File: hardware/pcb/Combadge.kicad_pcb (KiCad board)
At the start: 2 copper layers, 33.7 x 31 mm, 38 parts, among them J1 Conn_01x02_Socket, J2 Conn_01x01_Socket, J3 TOUCH, J4 USB_B_Micro, SW1 SW_Push, SW2 CSS-1210TB, U1 ESP32-WROOM-32, U2 MAX98357AETE+T, U3 MCP73831-2-OT, U4 TL431DBZ, U5 TLV73333PDBV

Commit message: Miscellaneous cleanup
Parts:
- renumbered BT to BT1
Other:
- board text added: "It is possible to commit no mistakes and still lose."
- board text added: "That is not a weakness; that is life."
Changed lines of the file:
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@@
     (property "ki_keywords" "battery cell")
     (attr through_hole)
-    (fp_text reference "BT" (at -2.433971 1.097635 63) (layer "F.SilkS")
+    (fp_text reference "BT1" (at -2.816662 0.066821 63) (layer "F.SilkS")
         (effects (font (size 1 1) (thickness 0.15)))
     )
@@
     (property "ki_keywords" "diode device shunt regulator")
     (attr smd)
-    (fp_text reference "U4" (at -0.0231 2.606) (layer "B.SilkS")
+    (fp_text reference "U4" (at -3.0203 1.0312) (layer "B.SilkS")
         (effects (font (size 1 1) (thickness 0.15)) (justify mirror))
     )
@@
     (property "ki_keywords" "R res resistor")
     (attr smd)
-    (fp_text reference "R2" (at -4.064 0 90) (layer "B.SilkS")
+    (fp_text reference "R2" (at -3.429 -0.4826 90) (layer "B.SilkS")
         (effects (font (size 1 1) (thickness 0.15)) (justify mirror))
     )
@@
     (effects (font (size 1 0.6) (thickness 0.15)) (justify mirror))
   )
+  (gr_text "That is not a weakness;\nthat is life." (at 157.9372 101.092) (layer "B.SilkS")
+    (effects (font (size 0.7 0.7) (thickness 0.16) bold) (justify left bottom mirror))
+  )
   (gr_text "+" (at 165.481 83.058 62) (layer "B.SilkS")
     (effects (font (size 0.8 0.8) (thickness 0.15)) (justify mirror))
@@
     (effects (font (size 0.8 0.8) (thickness 0.125)) (justify mirror))
   )
+  (gr_text "It is possible to\ncommit no mistakes\nand still lose." (at 156.0576 98.552) (layer "B.SilkS")
+    (effects (font (size 0.7 0.7) (thickness 0.16) bold) (justify left bottom mirror))
+  )
   (gr_text "\n+" (at 169.799 102.8446 -225) (layer "F.SilkS")
     (effects (font (size 1 1) (thickness 0.1)))
@@
   (segment (start 147.164 104.0294) (end 147.164 105.2409) (width 0.25) (layer "F.Cu") (net 3))
   (segment (start 160.2105 101.1555) (end 160.147 101.219) (width 0.25) (layer "F.Cu") (net 3))
+  (segment (start 153.2636 107.7468) (end 150.876 107.7468) (width 0.25) (layer "F.Cu") (net 3))
   (segment (start 160.147 101.219) (end 148.082 101.219) (width 0.25) (layer "F.Cu") (net 3))
   (segment (start 153.5445 106.5414) (end 157.443 106.5414) (width 0.25) (layer "F.Cu") (net 3))
+  (segment (start 150.876 109.3984) (end 150.876 107.7468) (width 0.25) (layer "F.Cu") (net 3))
   (segment (start 157.443 106.5414) (end 158.75 107.8484) (width 0.25) (layer "F.Cu") (net 3))
-  (segment (start 152.553 107.7214) (end 153.289 107.7214) (width 0.25) (layer "F.Cu") (net 3))
-  (segment (start 148.6285 107.1509) (end 150.876 109.3984) (width 0.25) (layer "F.Cu") (net 3))
   (segment (start 147.164 105.2409) (end 148.6285 106.7054) (width 0.25) (layer "F.Cu") (net 3))
   (segment (start 170.4594 93.345) (end 170.7896 93.6752) (width 0.25) (layer "F.Cu") (net 3))
   (segment (start 153.289 106.4129) (end 153.289 107.7214) (width 0.25) (layer "F.Cu") (net 3))
   (segment (start 170.7896 93.6752) (end 170.7896 94.5896) (width 0.25) (layer "F.Cu") (net 3))
+  (segment (start 153.289 107.7214) (end 153.2636 107.7468) (width 0.25) (layer "F.Cu") (net 3))
   (segment (start 153.289 106.2859) (end 153.5445 106.5414) (width 0.25) (layer "F.Cu") (net 3))
   (segment (start 169.0755 93.345) (end 170.4594 93.345) (width 0.25) (layer "F.Cu") (net 3))
   (segment (start 147.164 102.137) (end 147.164 104.0294) (width 0.25) (layer "F.Cu") (net 3))
-  (segment (start 148.6285 106.7054) (end 148.6285 107.1509) (width 0.25) (layer "F.Cu") (net 3))
-  (segment (start 150.876 109.3984) (end 152.553 107.7214) (width 0.25) (layer "F.Cu") (net 3))
+  (segment (start 149.6699 107.7468) (end 148.6285 106.7054) (width 0.25) (layer "F.Cu") (net 3))
   (segment (start 169.0755 93.345) (end 169.0755 95.758) (width 0.25) (layer "F.Cu") (net 3))
+  (segment (start 150.876 107.7468) (end 149.6699 107.7468) (width 0.25) (layer "F.Cu") (net 3))
   (segment (start 148.082 101.219) (end 147.164 102.137) (width 0.25) (layer "F.Cu") (net 3))
   (via (at 153.289 107.7214) (size 0.8) (drill 0.4) (layers "F.Cu" "B.Cu") (net 3))

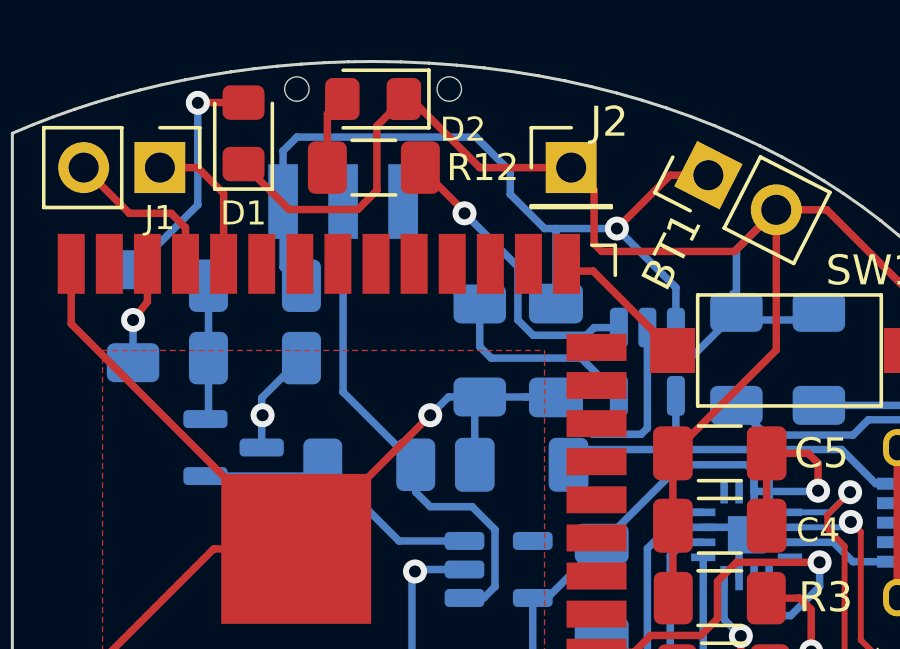
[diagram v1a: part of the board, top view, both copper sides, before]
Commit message: Rewire power switch so that the unit can be turned on
Thank you to Reddit user justadiode.
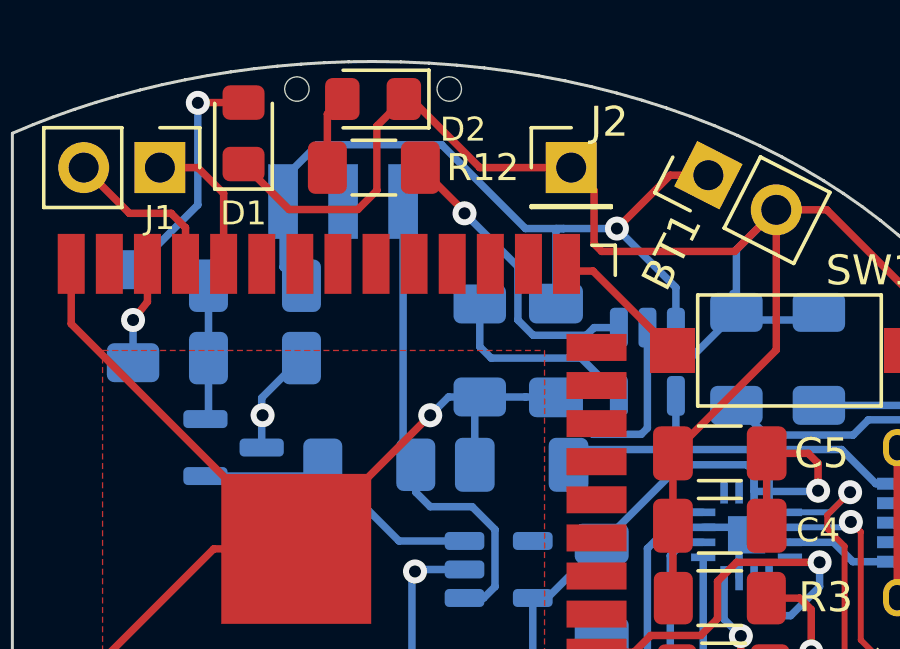
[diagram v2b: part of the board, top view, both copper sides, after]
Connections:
- SW2 pad 2: Net-(U5-IN) -> unconnected-(SW2-Pad2)
- SW2 pad 3: unconnected-(SW2-Pad3) -> Net-(U5-IN)
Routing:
- net +BATT: track 28.2 -> 27.2 mm
- net Net-(U5-IN): track 16.9 -> 16.1 mm

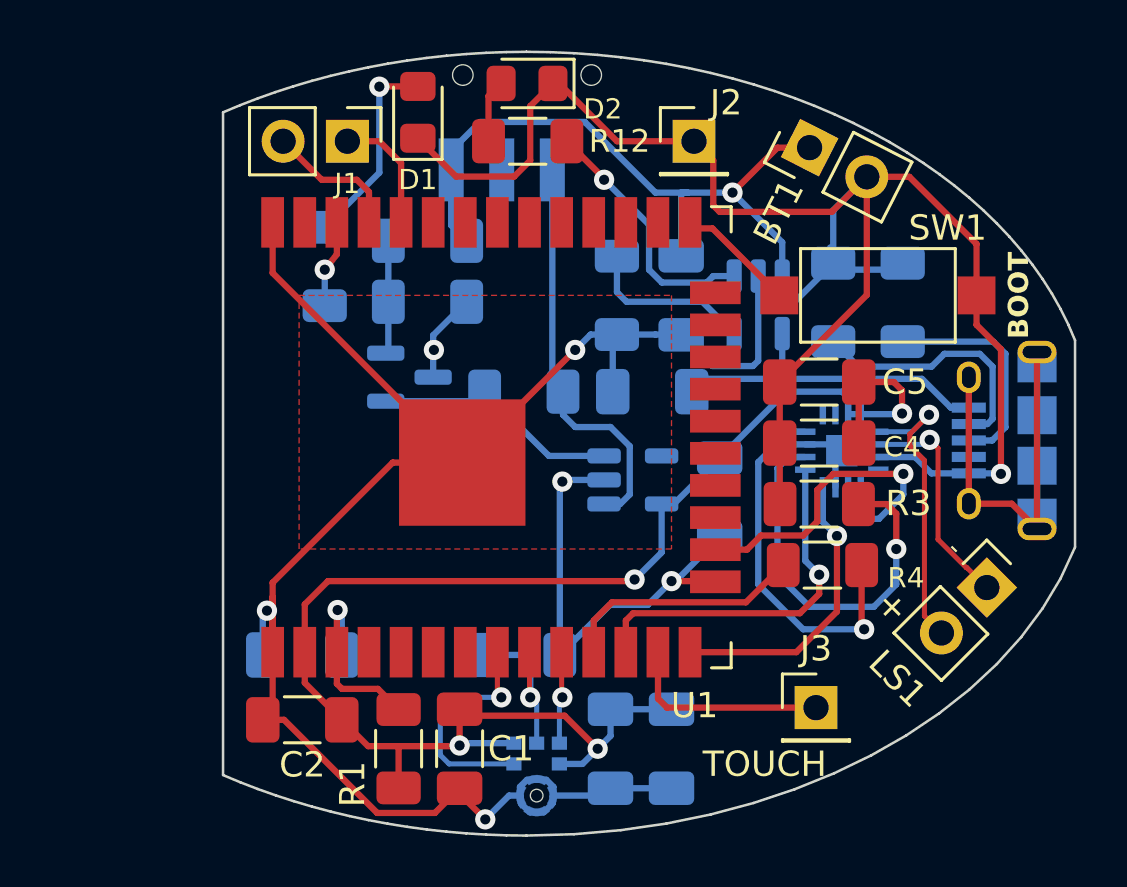
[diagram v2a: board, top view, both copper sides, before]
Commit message: Remove acute angles from PCB copper layers
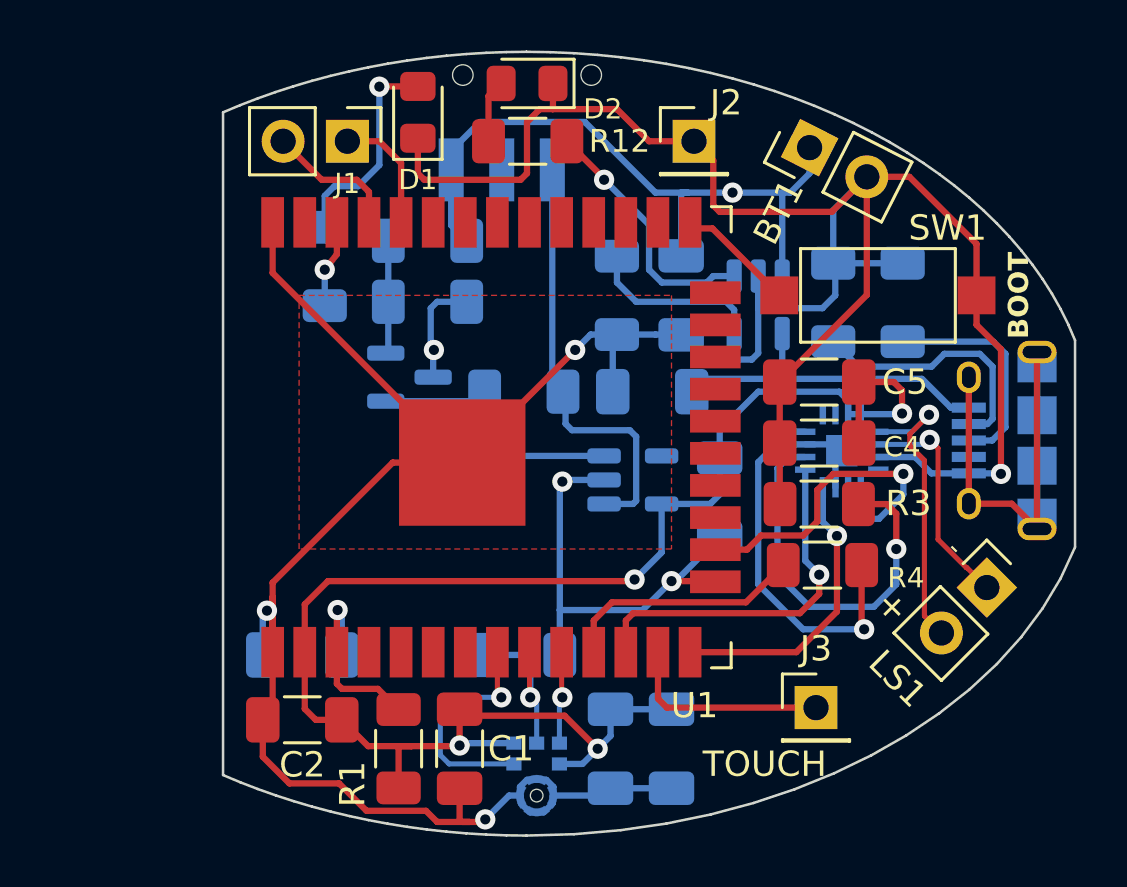
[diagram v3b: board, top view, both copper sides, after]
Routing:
- net GND: track 171.8 -> 175.5 mm
- net +3.3V: track 61.9 -> 64.4 mm
- net Net-(U4-K): track 9.84 -> 11.1 mm
- net Net-(U5-IN): track 16.1 -> 17.1 mm
- net /INDICATOR: track 8.11 -> 8.66 mm

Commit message: Update PCB from updated schematic
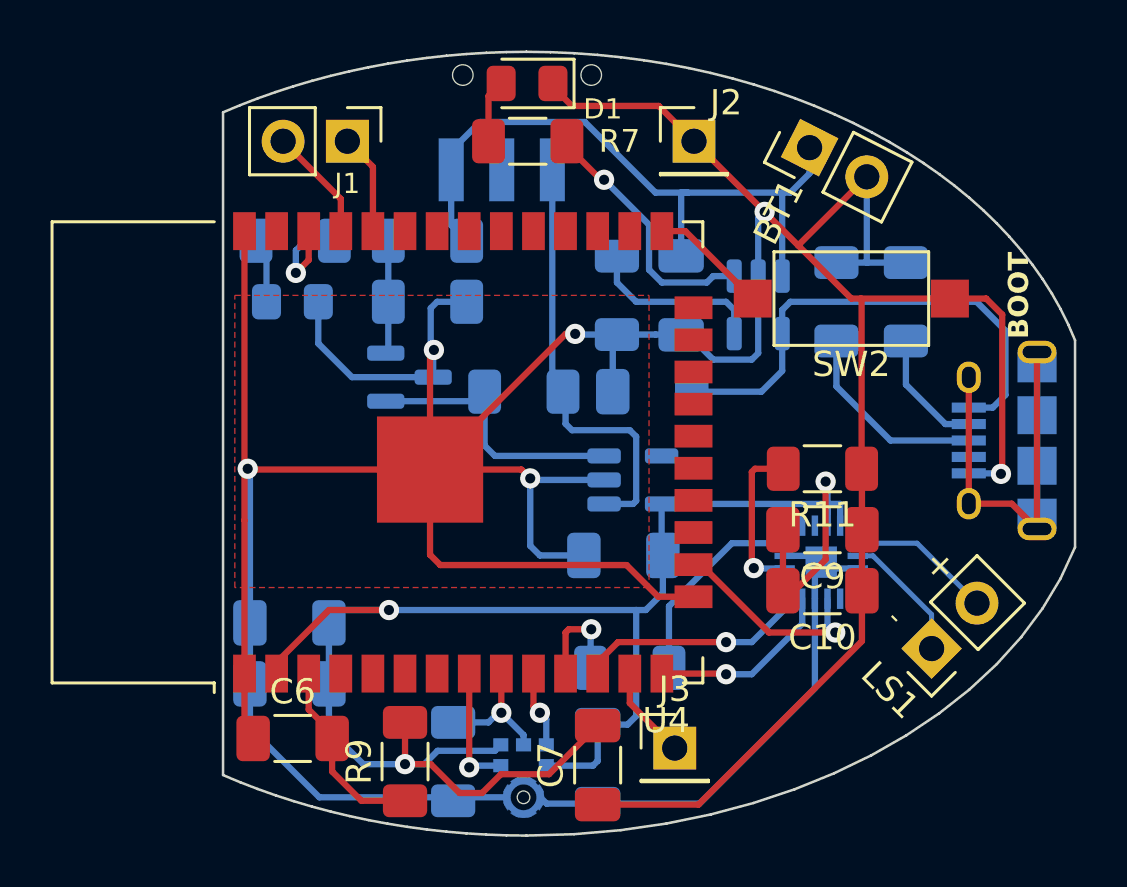
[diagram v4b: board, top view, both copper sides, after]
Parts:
- removed the C1 at (153.3, 107.8)
- removed the C2 at (147.1, 106.7)
- removed the C3 at (147.1, 104.1)
- removed the D1 at (151.6, 82.7)
- removed the R1 at (150.9, 107.8)
- removed the R2 at (148.0, 88.8)
- removed the R3 at (167.5, 98.2)
- removed the R4 at (167.6, 100.6)
- removed the R5 at (155.7, 104.1)
- removed the SW1 at (169.8, 89.9)
- removed the U1 at (154.1, 95.5)
- removed the U2 at (168.4, 96.1)
- added C10: 10uF, Capacitor_SMD:C_1206_3216Metric_Pad1.33x1.80mm_HandSolder, F.Cu at (167.6, 101.6)
- added C8: 0.1uF, Capacitor_SMD:C_1206_3216Metric_Pad1.33x1.80mm_HandSolder, B.Cu at (158.8, 108.5)
- added C9: 0.1uF, Capacitor_SMD:C_1206_3216Metric_Pad1.33x1.80mm_HandSolder, F.Cu at (167.6, 99.2)
- added D2: LED, LED_SMD:LED_0805_2012Metric_Pad1.15x1.40mm_HandSolder, B.Cu at (146.7, 90.2)
- added R10: 100k, Resistor_SMD:R_1206_3216Metric_Pad1.30x1.75mm_HandSolder, B.Cu at (153.0, 108.4)
- added R11: 100k, Resistor_SMD:R_1206_3216Metric_Pad1.30x1.75mm_HandSolder, F.Cu at (167.6, 96.8)
- added R12: 1k, Resistor_SMD:R_1206_3216Metric_Pad1.30x1.75mm_HandSolder, B.Cu at (160.0, 104.6)
- added R8: 100, Resistor_SMD:R_1206_3216Metric_Pad1.30x1.75mm_HandSolder, B.Cu at (146.8, 87.8)
- added R9: 10k, Resistor_SMD:R_1206_3216Metric_Pad1.30x1.75mm_HandSolder, F.Cu at (151.1, 108.4)
- added SW2: BOOT, Button_Switch_SMD:SW_SPST_CK_RS282G05A3, F.Cu at (168.8, 90.0)
- added U4: ESP32-WROOM-32, RF_Module:ESP32-WROOM-32, F.Cu at (153.0, 96.1)
- added U5: MAX98357AETE+T, MAX98357AETE+T:MAX98357AETE&plus_T, B.Cu at (167.6, 100.5)
- C4: value 0.1uF -> 10uF; moved to B.Cu
- C5: value 10uF -> 0.1uF; moved to B.Cu
- C6: value 0.1uF -> 10uF; moved to F.Cu
- C7: moved to F.Cu
- J1: value Conn_01x02_Socket -> UART
- J2: value Conn_01x01_Socket -> GND
- moved C5 24.1 mm to (146.6, 105.3)
- moved C4 22.1 mm to (146.6, 102.9)
- moved C6 12.6 mm to (146.7, 107.4), turned to 0 degrees
- moved J3 5.81 mm to (161.8, 107.8)
- moved C3 4.44 mm to (159.8, 100.2), turned to 180 degrees
- moved LS1 3.25 mm to (172.0, 103.9), turned to 135 degrees
- moved C7 2.99 mm to (158.8, 108.5)
- moved R1 2.88 mm to (170.9, 90.2), turned to -90 degrees
- moved R2 2.62 mm to (168.2, 90.2), turned to -90 degrees
- moved MK1 0.52 mm to (155.8, 109.1)
- renumbered C8 to C1, C9 to C2, C10 to C3, D2 to D1, R7 to R1, R6 to R2, R9 to R3, R10 to R4, R11 to R5, R8 to R6, R12 to R7, SW2 to SW1, U4 to U1, U3 to U2, U5 to U3
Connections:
- C6 pad 2: +3.3V -> Net-(U4-EN)
- J1 pad 1: /ESP_RX -> /ESP32/ESP_RX
- J1 pad 2: /ESP_TX -> /ESP32/ESP_TX
- J3 pad 1: Net-(J3-Pin_1) -> /ESP32/TOUCH
- LS1 pad 1: /SPK- -> /Speaker/SPK-
- LS1 pad 2: /SPK+ -> /Speaker/SPK+
- MK1 pad 2: /MIC_BCLK -> /ESP32/MIC_BCLK
- MK1 pad 5: /MIC_WS -> /ESP32/MIC_WS
- MK1 pad 6: /MIC_DATA -> /ESP32/MIC_DATA
- R1 pad 1: Net-(J4-D-) -> GND
- R1 pad 2: GND -> Net-(J4-D-)
- R2 pad 1: Net-(J4-D+) -> GND
- R2 pad 2: GND -> Net-(J4-D+)
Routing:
- net GND: track 175.5 -> 206.6 mm, vias 7 -> 6
- net /GAIN_SELECT: track 15.5 -> 0.00 mm, vias 1 -> 0
- net Net-(U2-*SD_MODE): track 14.7 -> 0.00 mm, vias 1 -> 0
- net /SPK_DATA: track 14.5 -> 0.00 mm, vias 1 -> 0
- net /SPK_WS: track 13.9 -> 0.00 mm, vias 1 -> 0
- net /SPK+: track 11.7 -> 0.00 mm, vias 1 -> 0
- net /SPK_BCLK: track 11.6 -> 0.00 mm, vias 1 -> 0
- net /ESP32/SPK_DATA: track 0.00 -> 9.82 mm, vias 0 -> 1
- net /SPK_EN: track 9.66 -> 0.00 mm
- net /MIC_BCLK: track 9.38 -> 0.00 mm, vias 1 -> 0
- net /SPK-: track 8.90 -> 0.00 mm, vias 1 -> 0
- net /INDICATOR: track 8.66 -> 0.00 mm, vias 1 -> 0
- net +3.3V: track 64.4 -> 72.9 mm, vias 4 -> 3
- net Net-(J3-Pin_1): track 8.23 -> 0.00 mm
- net /ESP32/SPK_WS: track 0.00 -> 8.18 mm, vias 0 -> 1
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
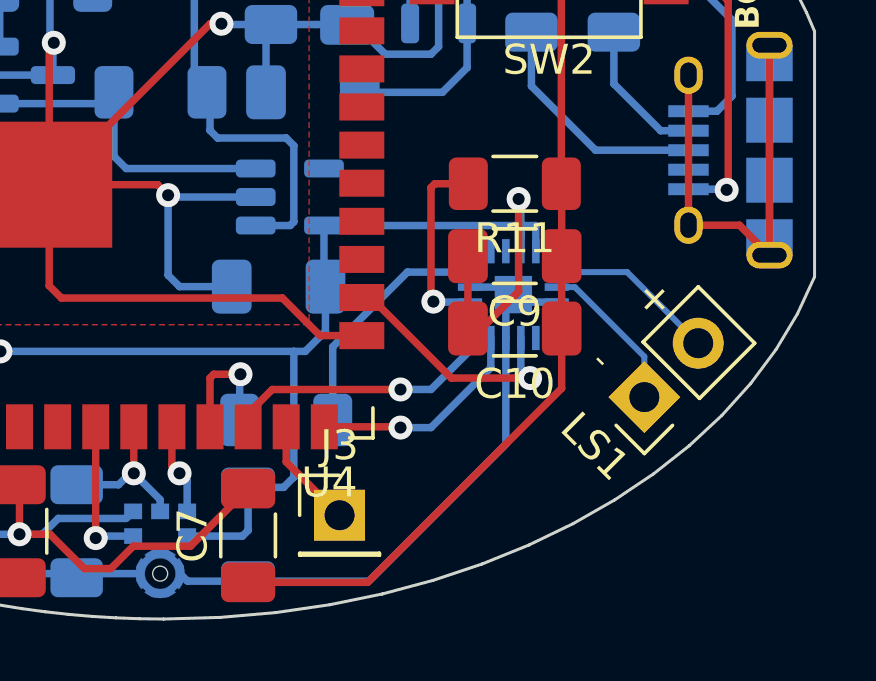
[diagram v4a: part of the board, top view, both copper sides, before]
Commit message: Replace third party MAX98357 symbol with custom one
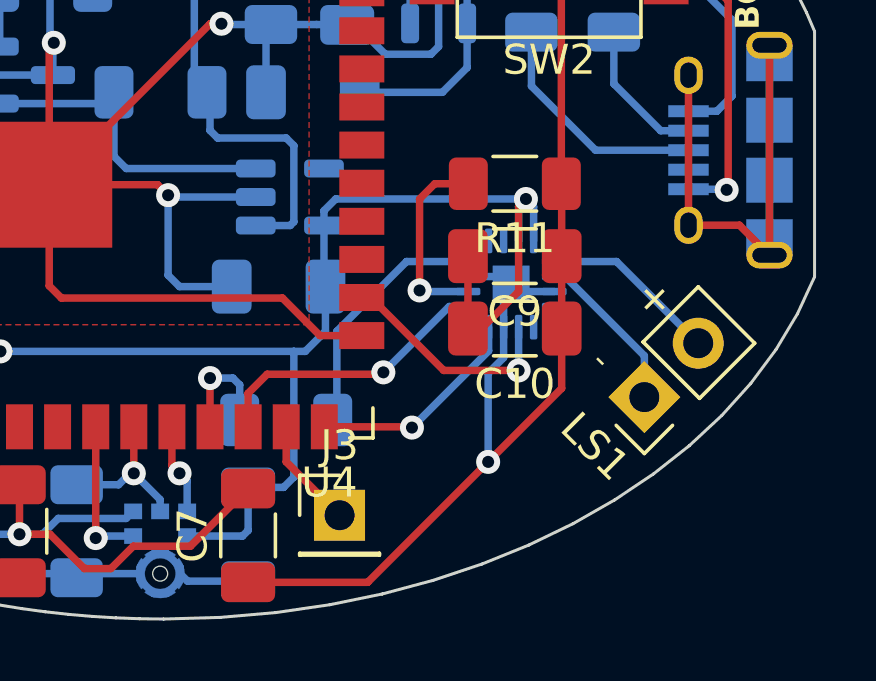
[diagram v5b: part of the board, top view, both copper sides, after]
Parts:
- U5: footprint MAX98357AETE+T:MAX98357AETE&plus_T -> Package_DFN_QFN:TQFN-16-1EP_3x3mm_P0.5mm_EP1.23x1.23mm
- moved U5 0.36 mm to (167.5, 100.1)
- turned R12 to 180 degrees
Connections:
- net /Speaker/SPK+ renamed Net-(U5-OUTP)
- net /Speaker/SPK- renamed Net-(U5-OUTN)
- R12 pad 1: /ESP32/SPK_EN -> Net-(U5-SD_MODE)
- R12 pad 2: Net-(U5-*SD_MODE) -> /ESP32/SPK_EN
- U5 pad 4: Net-(U5-*SD_MODE) -> Net-(U5-SD_MODE)
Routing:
- net GND: track 206.6 -> 197.2 mm, vias 6 -> 7
- net Net-(U5-SD_MODE): track 0.00 -> 8.35 mm
- net Net-(U5-*SD_MODE): track 8.05 -> 0.00 mm
- net /ESP32/SPK_WS: track 8.18 -> 7.68 mm
